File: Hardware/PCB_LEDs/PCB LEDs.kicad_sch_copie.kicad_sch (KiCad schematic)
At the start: 22 parts, among them J1 SCL, J2 SDA, J3 CLOCK, J4 OUTPUT, J5 POWER, U1 PCA9685PW

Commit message: pcb revue
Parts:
- removed D1: LED_RGBA, LED_SMD:LED_RGB_1210, symbol Device:LED_RGBA
- removed J1: SCL, Connector_JST:JST_XH_B2B-XH-A_1x02_P2.50mm_Vertical, symbol Connector_Generic:Conn_01x02
- removed J2: SDA, Connector_JST:JST_XH_B2B-XH-A_1x02_P2.50mm_Vertical, symbol Connector_Generic:Conn_01x02
- removed J3: CLOCK, Connector_JST:JST_XH_B2B-XH-A_1x02_P2.50mm_Vertical, symbol Connector_Generic:Conn_01x02
- removed J4: OUTPUT, Connector_JST:JST_XH_B2B-XH-A_1x02_P2.50mm_Vertical, symbol Connector_Generic:Conn_01x02
- removed J5: POWER, Connector_JST:JST_XH_B2B-XH-A_1x02_P2.50mm_Vertical, symbol Connector_Generic:Conn_01x02
- added D1: LED_RGB, LED_SMD:LED_Avago_PLCC6_3x2.8mm, symbol Device:LED_RGB
- added J1: Conn_01x05, Connector_JST:JST_XH_B5B-XH-A_1x05_P2.50mm_Vertical, symbol Connector_Generic:Conn_01x05
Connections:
- net +5V: now also J1.5 (Pin_5)
- net GND: now also J1.1 (Pin_1)
- net OUTPUT: now also J1.2 (Pin_2)
- net SCL: now also J1.3 (Pin_3)
- net SDA: now also J1.4 (Pin_4)
- net at R7.1: now also D1.1 (RK)
- net at R5.1: now also D1.2 (GK)
- net at R6.1: now also D1.3 (BK)
- net at U1.6 (LED0): now also D1.4 (BA)
- net at U1.7 (LED1): now also D1.5 (GA)
- net at U1.8 (LED2): now also D1.6 (RA)
- net EXTERNAL_CLOCK: no longer names the net of U1.25 (EXTCLK)
- no-connect marks 17 -> 16

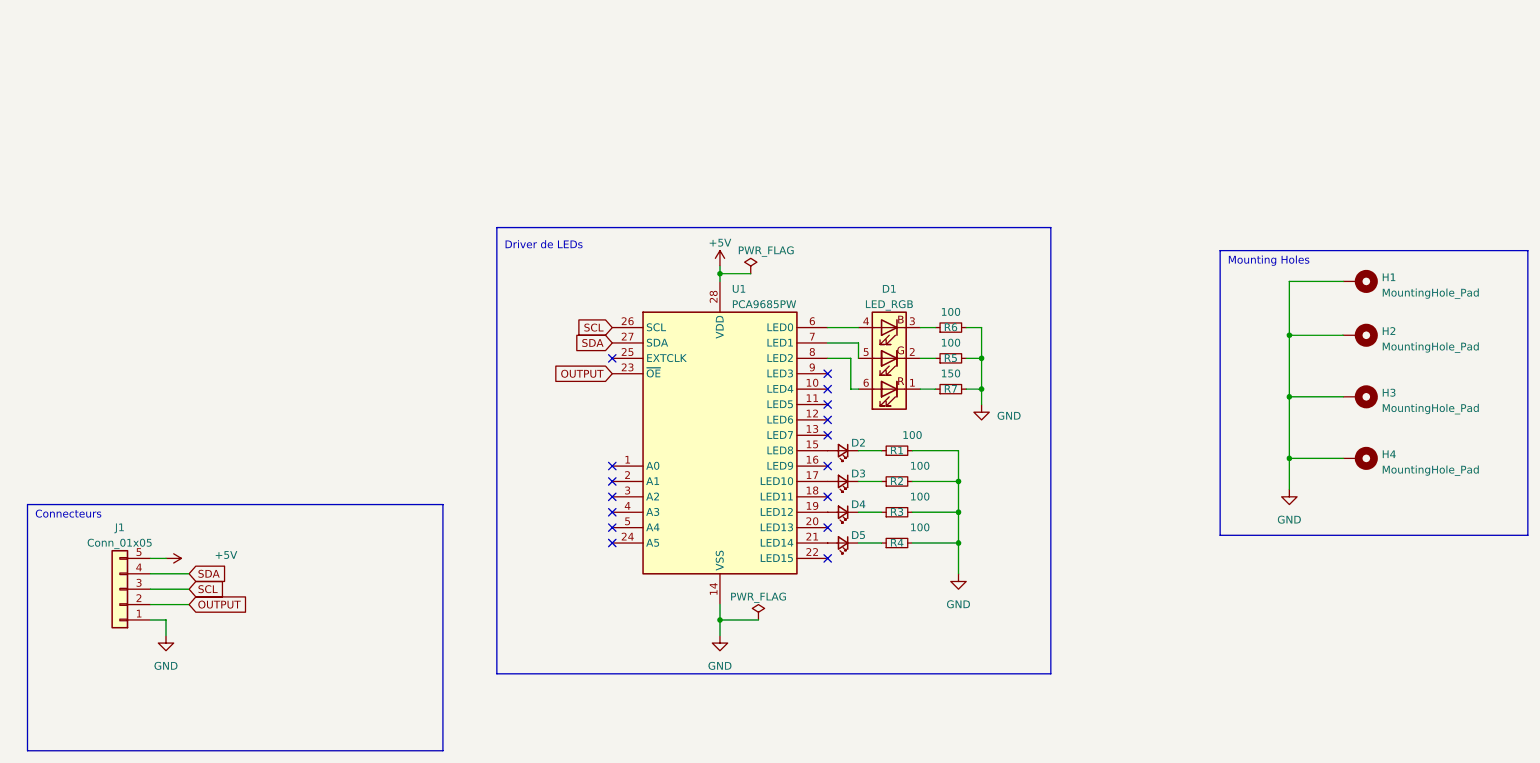
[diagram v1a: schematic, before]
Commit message: Correction des erreurs après amphi
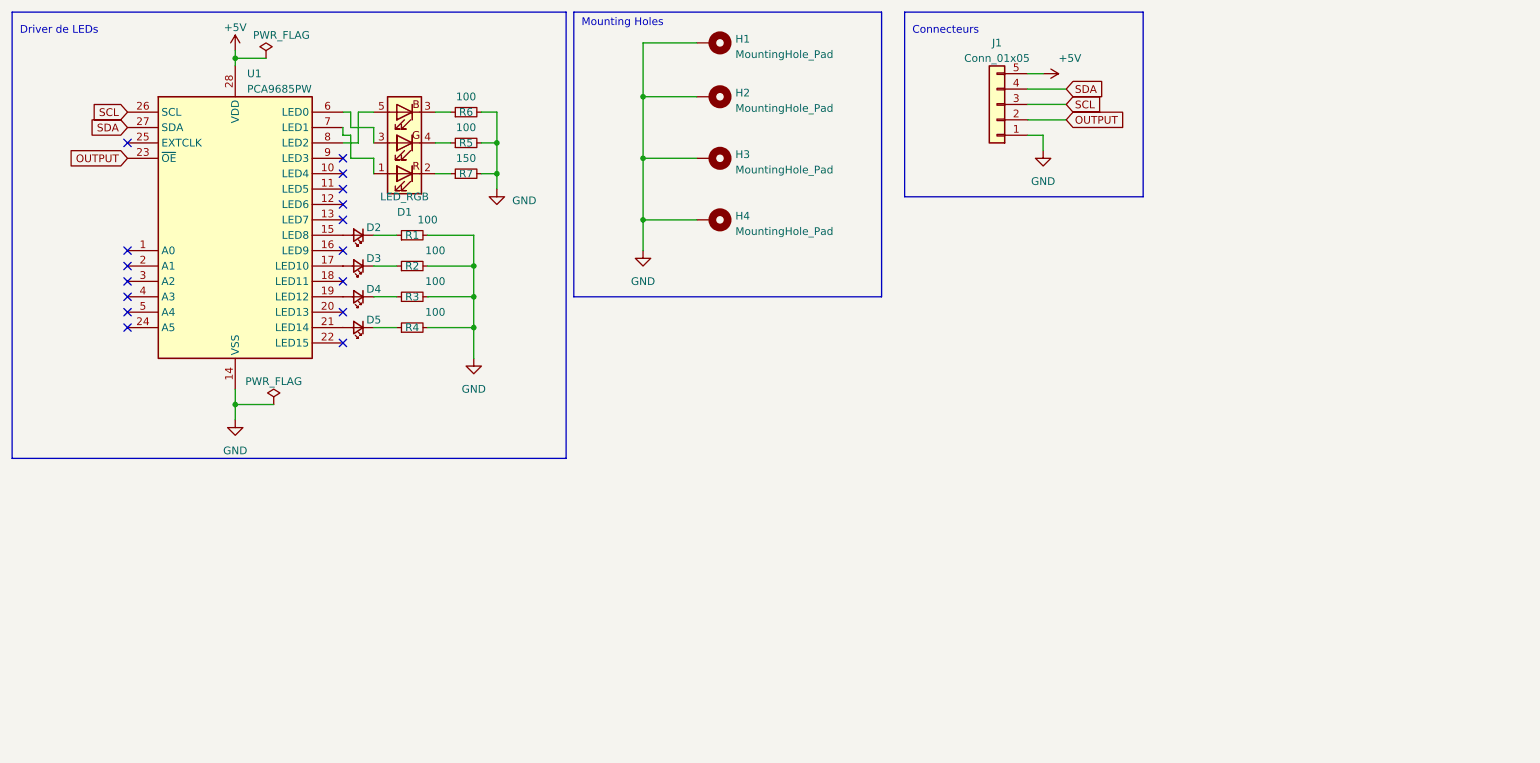
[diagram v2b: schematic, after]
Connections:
- net at R7.1: now also D1.2 (RK); no longer D1.1 (RK)
- net at R5.1: now also D1.4 (GK); no longer D1.2 (GK)
- net at U1.6 (LED0): now also D1.3 (GK); no longer D1.4 (BA)
- net at U1.7 (LED1): now also D1.1 (RA); no longer D1.5 (GA)
- net at U1.8 (LED2): now also D1.5 (BA); no longer D1.6 (RA)
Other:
- moved on the sheet: D1, D2, D3, D4, D5, H1, H2, H3, H4, J1, R1, R2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

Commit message: Correction erreurs V2
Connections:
- net at D1.3 (GK): now also U1.6 (LED0); no longer R6.1
- new net: D1.6, R6.1
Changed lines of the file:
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@@
   (symbol (lib_id "Device:LED_RGB") (at 78.74 35.56 180) (unit 1)
     (in_bom yes) (on_board yes) (dnp no) (fields_autoplaced)
-    (property "Reference" "D1" (at 78.74 46.99 0)
+    (property "Reference" "D1" (at 78.74 24.13 0)
       (effects (font (size 1.27 1.27)))
     )
-    (property "Value" "LED_RGB" (at 78.74 44.45 0)
+    (property "Value" "LED_RGB" (at 78.74 26.67 0)
       (effects (font (size 1.27 1.27)))
     )
-    (property "Footprint" "LED_SMD:LED_Avago_PLCC6_3x2.8mm" (at 78.74 36.83 0)
+    (property "Footprint" "LED_SMD:LED_Avago_PLCC6_3x2.8mm" (at 78.74 34.29 0)
       (effects (font (size 1.27 1.27)) hide)
     )
-    (property "Datasheet" "~" (at 78.74 36.83 0)
+    (property "Datasheet" "~" (at 78.74 34.29 0)
       (effects (font (size 1.27 1.27)) hide)
     )
+    (pin "1")
     (pin "2")
+    (pin "6")
+    (pin "3")
     (pin "4")
-    (pin "3")
     (pin "5")
-    (pin "3")
-    (pin "1")
     (instances
       (project "PCB LEDs.kicad_sch_copie"
